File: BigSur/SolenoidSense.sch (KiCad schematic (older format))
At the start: 34 parts, among them U10 MCP6L02T-E_MS, U11 74LVC1G00W5-7, U12 ACS70331EESATR-2P5U3, U5 ACS70331EESATR-2P5U3, U6 ACS70331EESATR-2P5U3, U7 ACS70331EESATR-2P5U3, U8 ACS70331EESATR-2P5U3, U9 ACS70331EESATR-2P5U3

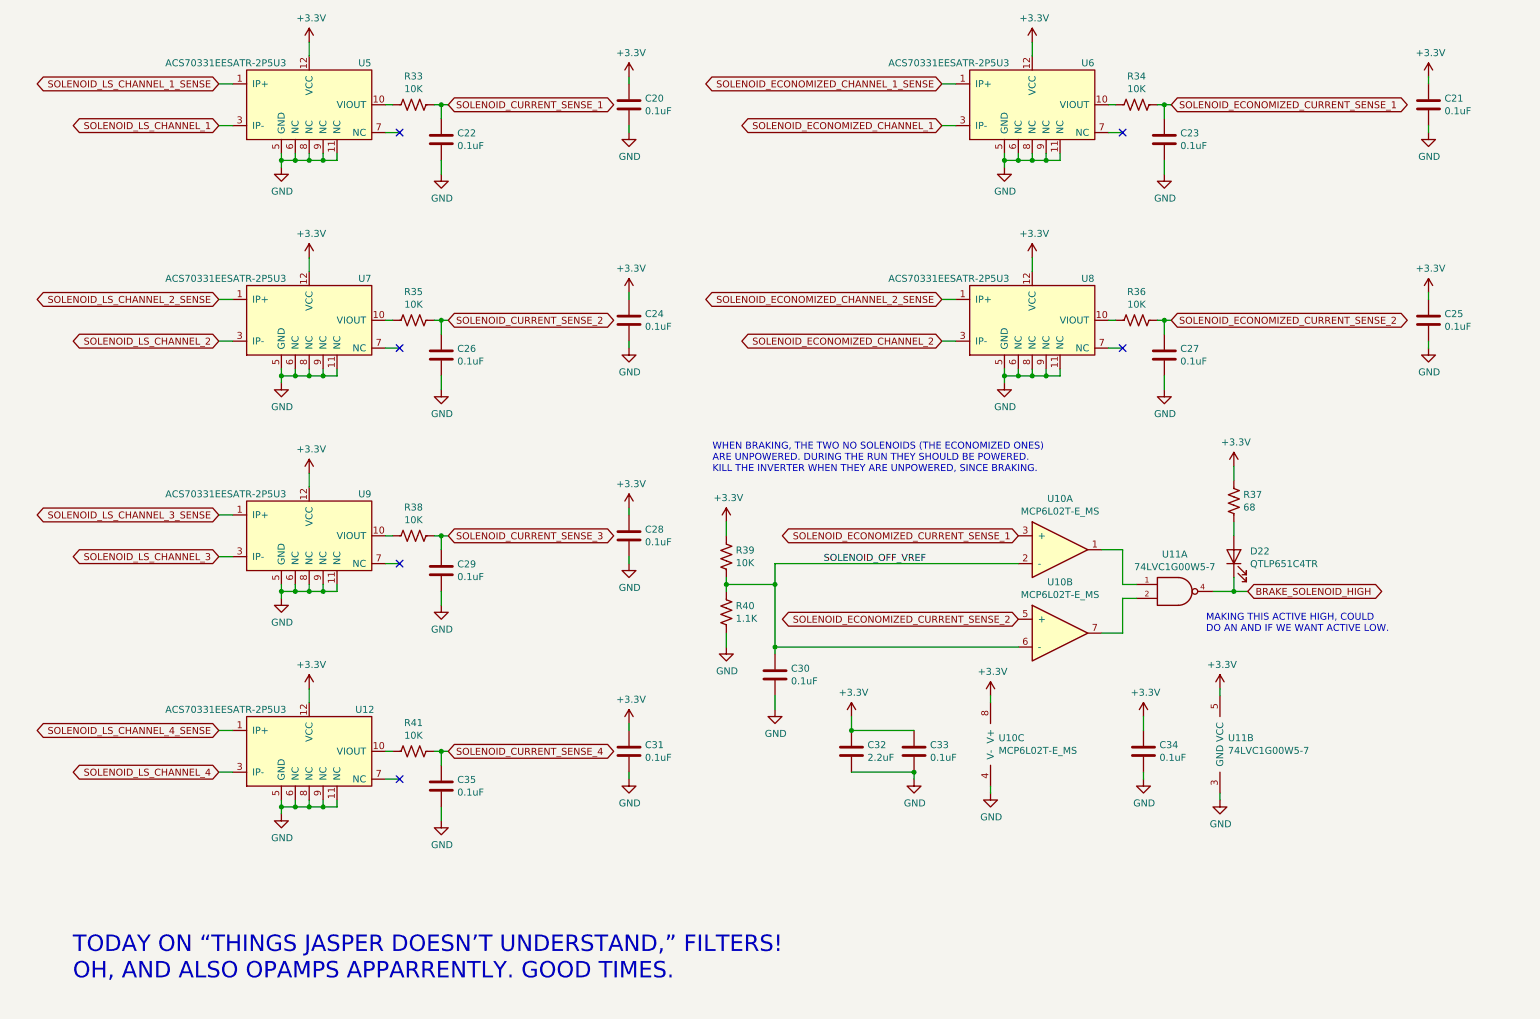
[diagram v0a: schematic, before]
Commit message: Switched to active low brake lines
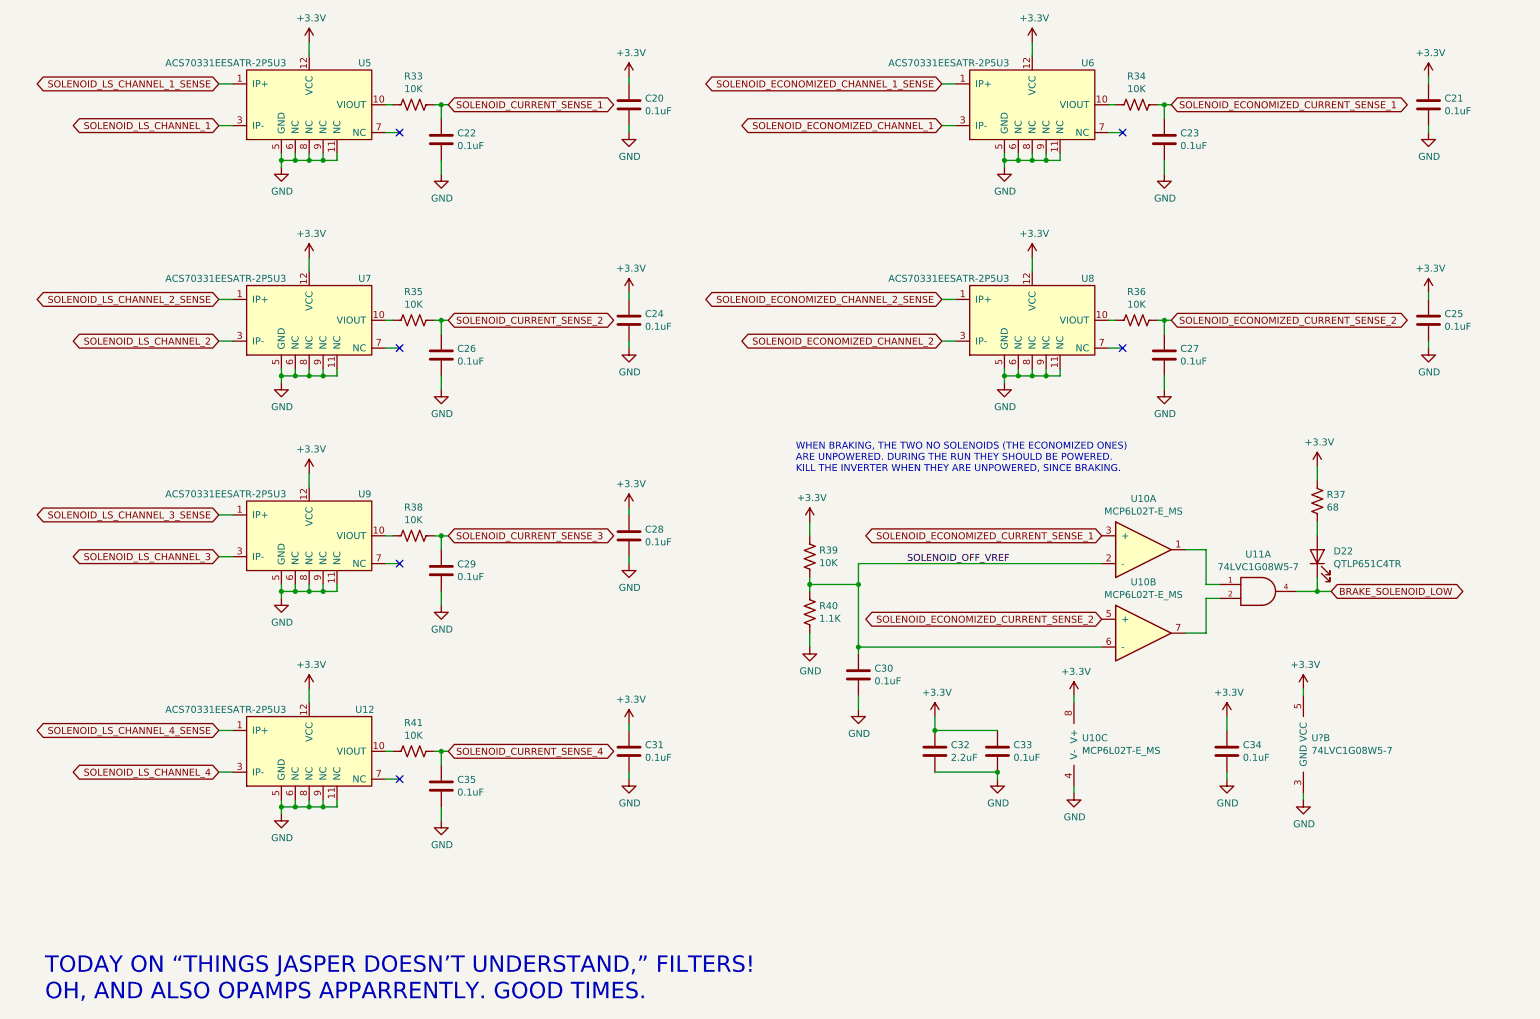
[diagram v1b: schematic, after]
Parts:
- removed U11: 74LVC1G00W5-7, Package_TO_SOT_SMD:SOT-23-5, symbol BigSurLib:74LVC1G00W5-7
- added U11, U?: 74LVC1G08W5-7, Package_TO_SOT_SMD:SOT-23-5, symbol BigSurLib:74LVC1G08W5-7
- R39: Digikey RNCP0603FTD10K0 -> https://www.digikey.ca/product-detail/en/stackpole-electron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; Part Number https://www.digikey.ca/product-detail/en/stackpole-electron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 -> RNCP0603FTD10K0
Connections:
- net +3V3: now also U?.5 (VCC)
- net GND: now also U?.3 (GND)
- net at U10.1: now also U11.1
- net at U10.7: now also U11.2
- net BRAKE_SOLENOID_HIGH renamed BRAKE_SOLENOID_LOW
- net BRAKE_SOLENOID_LOW: now also U11.4
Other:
- note removed: "MAKING THIS ACTIVE HIGH, COULD\nDO AN AND IF WE WANT ACTIVE LOW."
- moved on the sheet: C30, C32, C33, C34, D22, R37, R39, R40, U10A, U10B, U10C

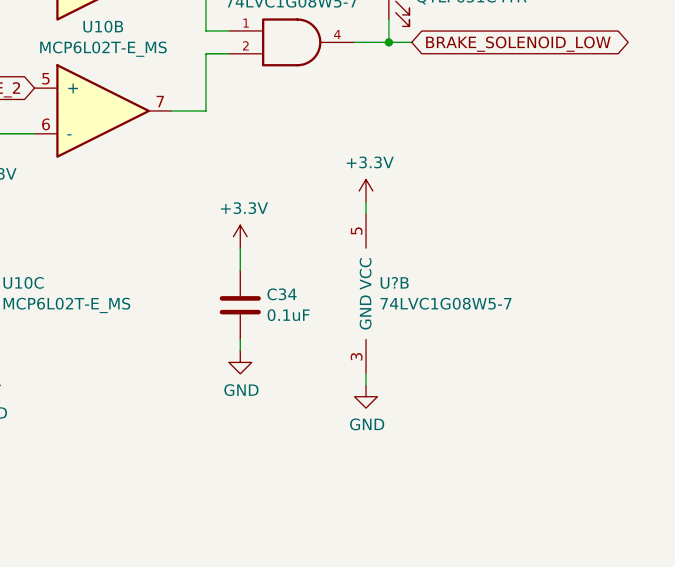
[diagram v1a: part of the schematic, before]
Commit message: Generate netlist, started some very rough placement
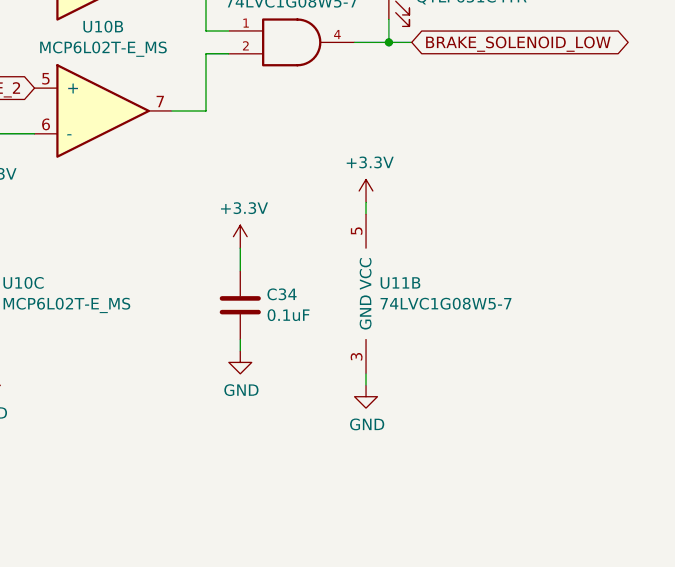
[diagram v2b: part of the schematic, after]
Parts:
- gave numbers to parts that had none: 1
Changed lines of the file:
@@
 $EndComp
 $Comp
-L BigSurLib:74LVC1G08W5-7 U?
+L BigSurLib:74LVC1G08W5-7 U11
 U 2 1 5DD4ED6F
 P 9650 5850
-F 0 "U?" H 9708 5896 50  0000 L CNN
+F 0 "U11" H 9708 5896 50  0000 L CNN
 F 1 "74LVC1G08W5-7" H 9708 5805 50  0000 L CNN
 F 2 "Package_TO_SOT_SMD:SOT-23-5" H 9700 6050 50  0001 C CNN
-F 3 "https://www.diodes.com/assets/Datasheets/74LVC1G00.pdf" H 9700 5850 50  0001 C CNN
+F 3 "https://www.diodes.com/assets/Datasheets/74LVC1G08.pdf" H 9700 5850 50  0001 C CNN
 F 4 "https://www.digikey.ca/product-detail/en/diodes-incorporated/74LVC1G00W5-7/1034-74LVC1G00W5-7DICT-ND/5629187" H 9900 6150 50  0001 C CNN "Digikey"
 	2    9650 5850

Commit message: Made brake output active high in accordance with meeting decision
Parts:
- removed unit 1 of U11
- added unit 1 of U11
- U11: value 74LVC1G08W5-7 -> 74LVC1G00W5-7; symbol BigSurLib:74LVC1G08W5-7 -> BigSurLib:74LVC1G00W5-7
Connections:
- net BRAKE_SOLENOID_LOW: now also U11.4
- net at U10.1: now also U11.1
- net at U10.7: now also U11.2
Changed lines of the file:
@@
 EESchema Schematic File Version 4
 LIBS:BigSur-cache
-EELAYER 29 0
+EELAYER 30 0
 EELAYER END
 $Descr A4 11693 8268
@@
 	9050 4800 8950 4800
 $Comp
-L BigSurLib:74LVC1G08W5-7 U11
-U 1 1 5DD472CB
-P 9300 4750
-F 0 "U11" H 9325 5017 50  0000 C CNN
-F 1 "74LVC1G08W5-7" H 9325 4926 50  0000 C CNN
-F 2 "Package_TO_SOT_SMD:SOT-23-5" H 9350 4950 50  0001 C CNN
-F 3 "https://www.diodes.com/assets/Datasheets/74LVC1G08.pdf" H 9350 4750 50  0001 C CNN
-F 4 "https://www.digikey.ca/product-detail/en/diodes-incorporated/74LVC1G08W5-7/74LVC1G08W5-7DICT-ND/2330117" H 9550 5050 50  0001 C CNN "Digikey"
-	1    9300 4750
-	1    0    0    -1
-$EndComp
-$Comp
-L BigSurLib:74LVC1G08W5-7 U11
+L BigSurLib:74LVC1G00W5-7 U11
 U 2 1 5DD4ED6F
 P 9650 5850
 F 0 "U11" H 9708 5896 50  0000 L CNN
-F 1 "74LVC1G08W5-7" H 9708 5805 50  0000 L CNN
+F 1 "74LVC1G00W5-7" H 9708 5805 50  0000 L CNN
 F 2 "Package_TO_SOT_SMD:SOT-23-5" H 9700 6050 50  0001 C CNN
 F 3 "https://www.diodes.com/assets/Datasheets/74LVC1G08.pdf" H 9700 5850 50  0001 C CNN
@@
 	1    0    0    -1
 $EndComp
+$Comp
+L BigSurLib:74LVC1G00W5-7 U11
+U 1 1 5DCDC7D8
+P 9300 4750
+F 0 "U11" H 9325 5017 50  0000 C CNN
+F 1 "74LVC1G00W5-7" H 9325 4926 50  0000 C CNN
+F 2 "Package_TO_SOT_SMD:SOT-23-5" H 9350 4950 50  0001 C CNN
+F 3 "https://www.diodes.com/assets/Datasheets/74LVC1G08.pdf" H 9350 4750 50  0001 C CNN
+F 4 "https://www.digikey.ca/product-detail/en/diodes-incorporated/74LVC1G00W5-7/1034-74LVC1G00W5-7DICT-ND/5629187" H 9550 5050 50  0001 C CNN "Digikey"
+	1    9300 4750
+	1    0    0    -1
+$EndComp

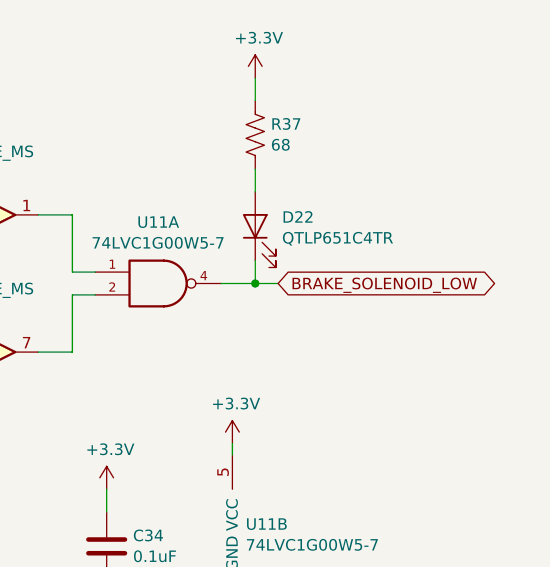
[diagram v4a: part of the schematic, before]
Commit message: Squished output connectors together, going to need to fix layout.
Also still needs CAN and inverter chill connectors.
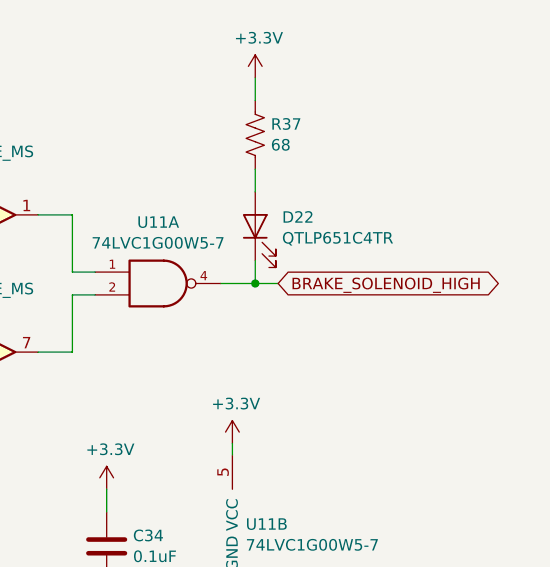
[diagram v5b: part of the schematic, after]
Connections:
- net BRAKE_SOLENOID_LOW renamed BRAKE_SOLENOID_HIGH
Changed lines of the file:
@@
 EESchema Schematic File Version 4
 LIBS:BigSur-cache
-EELAYER 30 0
+EELAYER 29 0
 EELAYER END
 $Descr A4 11693 8268
@@
 	9100 5650 9100 5750
 Text GLabel 9850 4750 2    50   BiDi ~ 0
-BRAKE_SOLENOID_LOW
+BRAKE_SOLENOID_HIGH
 $Comp
 L BigSurLib:ACS70331EESATR-2P5U3 U5
